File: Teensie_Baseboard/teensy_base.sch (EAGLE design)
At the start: 9 parts, among them IC1 7805T

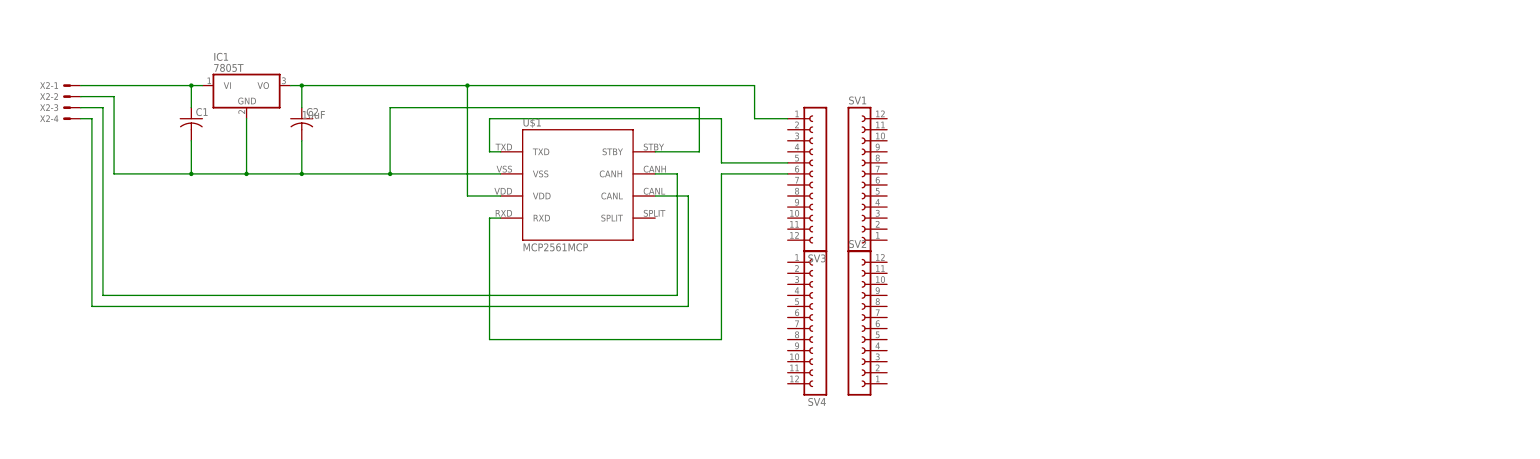
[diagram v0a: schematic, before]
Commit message: Some cleanup, added Arduino Pro Mini as a placeholder for the data collectors
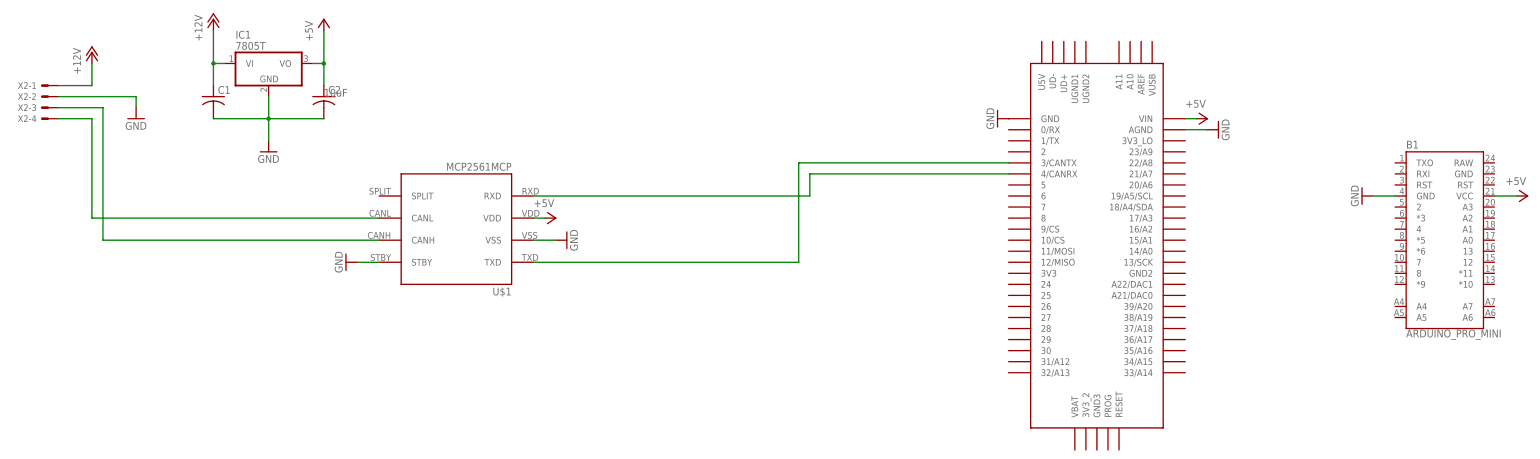
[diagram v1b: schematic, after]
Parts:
- removed SV1, SV2, SV3, SV4: (no value), con-lsta:FE12-1
- added B1: ARDUINO_PRO_MINI, SparkFun-Boards:ARDUINO_PRO_MINI
- added U$2: TEENSY_3.5/3.6, Teensy356:TEENSY_3.5/3.6
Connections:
- net N$1 renamed +12V
- removed net 5V: C2.1, IC1.VO, SV3.1, U$1.VDD
- removed net GROUND: C1.2, C2.2, IC1.GND, U$1.STBY, U$1.VSS, X2-2.S
- removed net N$3: SV3.5, U$1.TXD
- removed net N$4: SV3.6, U$1.RXD
- new net +5V: B1.VCC, C2.1, IC1.VO, U$1.VDD, U$2.VIN
- new net GND: B1.GND, C1.2, C2.2, IC1.GND, U$1.STBY, U$1.VSS, U$2.AGND, U$2.GND, X2-2.S
- new net N$1: U$1.RXD, U$2.4/CANRX
- new net N$2: U$1.TXD, U$2.3/CANTX
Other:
- moved on the sheet: C1, C2, IC1, U$1, X2-1, X2-2, X2-3, X2-4
